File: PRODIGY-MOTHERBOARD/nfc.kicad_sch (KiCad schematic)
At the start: 1 part, among them U14 PN5321A3HN_C1xx

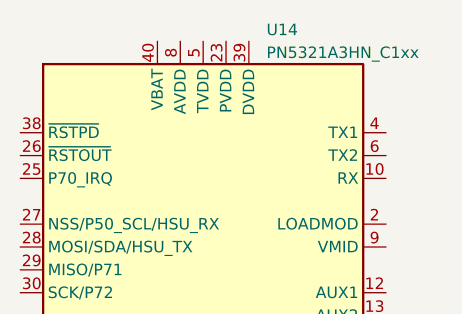
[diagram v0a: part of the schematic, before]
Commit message: project restructure done. Hierarchical sheet done. Outputs/breakouts sheet done
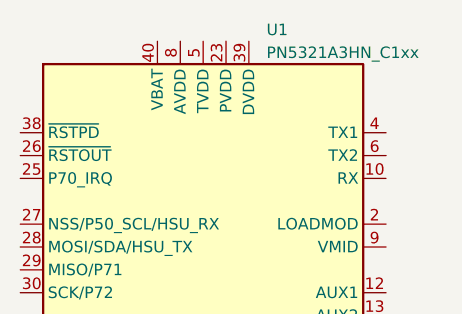
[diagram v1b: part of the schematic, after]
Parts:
- renumbered U14 to U1
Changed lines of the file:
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@@
-(kicad_sch (version 20230121) (generator eeschema)
-  (paper "A4")
-  (symbol (lib_id "RF_NFC:PN5321A3HN_C1xx") (at 148.59 95.25 0) (unit 1)
-    (in_bom yes) (on_board yes) (dnp no) (fields_autoplaced)
-    (property "Reference" "U14" (at 155.6259 60.96 0)
-      (effects (font (size 1.27 1.27)) (justify left))
-    )
-    (property "Value" "PN5321A3HN_C1xx" (at 155.6259 63.5 0)
-      (effects (font (size 1.27 1.27)) (justify left))
-    )
-    (property "Footprint" "Package_DFN_QFN:HVQFN-40-1EP_6x6mm_P0.5mm_EP4.1x4.1mm" (at 186.69 127 0)
-      (effects (font (size 1.27 1.27)) hide)
-    )
-    (property "Datasheet" "https://www.nxp.com/docs/en/nxp/data-sheets/PN532_C1.pdf" (at 148.59 90.17 0)
-      (effects (font (size 1.27 1.27)) hide)
-    )
-    (pin "1")
-    (pin "10")
-    (pin "11")
-    (pin "12")
-    (pin "13")
-    (pin "14")
-    (pin "15")
-    (pin "16")
-    (pin "17")
-    (pin "18")
-    (pin "19")
-    (pin "2")
-    (pin "20")
-    (pin "21")
-    (pin "22")
-    (pin "23")
-    (pin "24")
-    (pin "25")
-    (pin "26")
-    (pin "27")
-    (pin "28")
-    (pin "29")
-    (pin "3")
-    (pin "30")
-    (pin "31")
-    (pin "32")
-    (pin "33")
-    (pin "34")
-    (pin "35")
-    (pin "36")
-    (pin "37")
-    (pin "38")
-    (pin "39")
-    (pin "4")
-    (pin "40")
-    (pin "41")
-    (pin "5")
-    (pin "6")
-    (pin "7")
-    (pin "8")
-    (pin "9")
-    (instances
-      (project "PRODIGY-MOTHERBOARD"
-        (path "/f1c25860-8989-4190-bd24-2491d23ca7d9/edf7e11a-2a6c-4bff-b9f6-56b011438f63"
-          (reference "U14") (unit 1)
-        )
-      )
-    )
-  )
+(kicad_sch
+	(version 20231120)
+	(generator "eeschema")
+	(generator_version "8.0")
+	(paper "A4")
+	(symbol
+		(lib_id "RF_NFC:PN5321A3HN_C1xx")
+		(at 148.59 95.25 0)
+		(unit 1)
+		(exclude_from_sim no)
+		(in_bom yes)
+		(on_board yes)
+		(dnp no)
+		(fields_autoplaced yes)
+		(property "Reference" "U1"
+			(at 155.6259 60.96 0)
+			(effects
+				(font
+					(size 1.27 1.27)
+				)
+				(justify left)
+			)
+		)
+		(property "Value" "PN5321A3HN_C1xx"
+			(at 155.6259 63.5 0)
+			(effects
+				(font
+					(size 1.27 1.27)
+				)
+				(justify left)
+			)
+		)
+		(property "Footprint" "Package_DFN_QFN:HVQFN-40-1EP_6x6mm_P0.5mm_EP4.1x4.1mm"
+			(at 186.69 127 0)
+			(effects
+				(font
+					(size 1.27 1.27)
+				)
+				(hide yes)
+			)
+		)
+		(property "Datasheet" "https://www.nxp.com/docs/en/nxp/data-sheets/PN532_C1.pdf"
+			(at 148.59 90.17 0)
+			(effects
+				(font
+					(size 1.27 1.27)
+				)
+				(hide yes)
+			)
+		)
+		(property "Description" ""
+			(at 148.59 95.25 0)
+			(effects
+				(font
+					(size 1.27 1.27)
+				)
+				(hide yes)
+			)
+		)
+		(pin "1"
+		)
+		(pin "10"
+		)
+		(pin "11"
+		)
+		(pin "12"
+		)
+		(pin "13"
+		)
+		(pin "14"
+		)
+		(pin "15"
+		)
+		(pin "16"
+		)
+		(pin "17"
+		)
+		(pin "18"
+		)
+		(pin "19"
+		)
+		(pin "2"
+		)
+		(pin "20"
+		)
+		(pin "21"
+		)
+		(pin "22"
+		)
+		(pin "23"
+		)
+		(pin "24"
+		)
+		(pin "25"
+		)
+		(pin "26"
+		)
+		(pin "27"
+		)
+		(pin "28"
+		)
+		(pin "29"
+		)
+		(pin "3"
+		)
+		(pin "30"
+		)
+		(pin "31"
+		)
+		(pin "32"
+		)
+		(pin "33"
+		)
+		(pin "34"
+		)
+		(pin "35"
+		)
+		(pin "36"
+		)
+		(pin "37"
+		)
+		(pin "38"
+		)
+		(pin "39"
+		)
+		(pin "4"
+		)
+		(pin "40"
+		)
+		(pin "41"
+		)
+		(pin "5"
+		)
+		(pin "6"
+		)
+		(pin "7"
+		)
+		(pin "8"
+		)
+		(pin "9"
+		)
+		(instances
+			(project "PRODIGY-MOTHERBOARD"
+				(path "/f1c25860-8989-4190-bd24-2491d23ca7d9/e2913798-f444-47a6-8b64-53020d7d816b/f75fe182-3b01-43c3-81e9-1a0709fd1be7"
+					(reference "U1")
+					(unit 1)
+				)
+			)
+		)
+	)
 )

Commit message: CAN schematic done
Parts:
- renumbered U1 to U3
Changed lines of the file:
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@@
 		(dnp no)
 		(fields_autoplaced yes)
-		(property "Reference" "U1"
+		(property "Reference" "U3"
 			(at 155.6259 60.96 0)
 			(effects
@@
 			(project "PRODIGY-MOTHERBOARD"
 				(path "/f1c25860-8989-4190-bd24-2491d23ca7d9/e2913798-f444-47a6-8b64-53020d7d816b/f75fe182-3b01-43c3-81e9-1a0709fd1be7"
-					(reference "U1")
+					(reference "U3")
 					(unit 1)
 				)

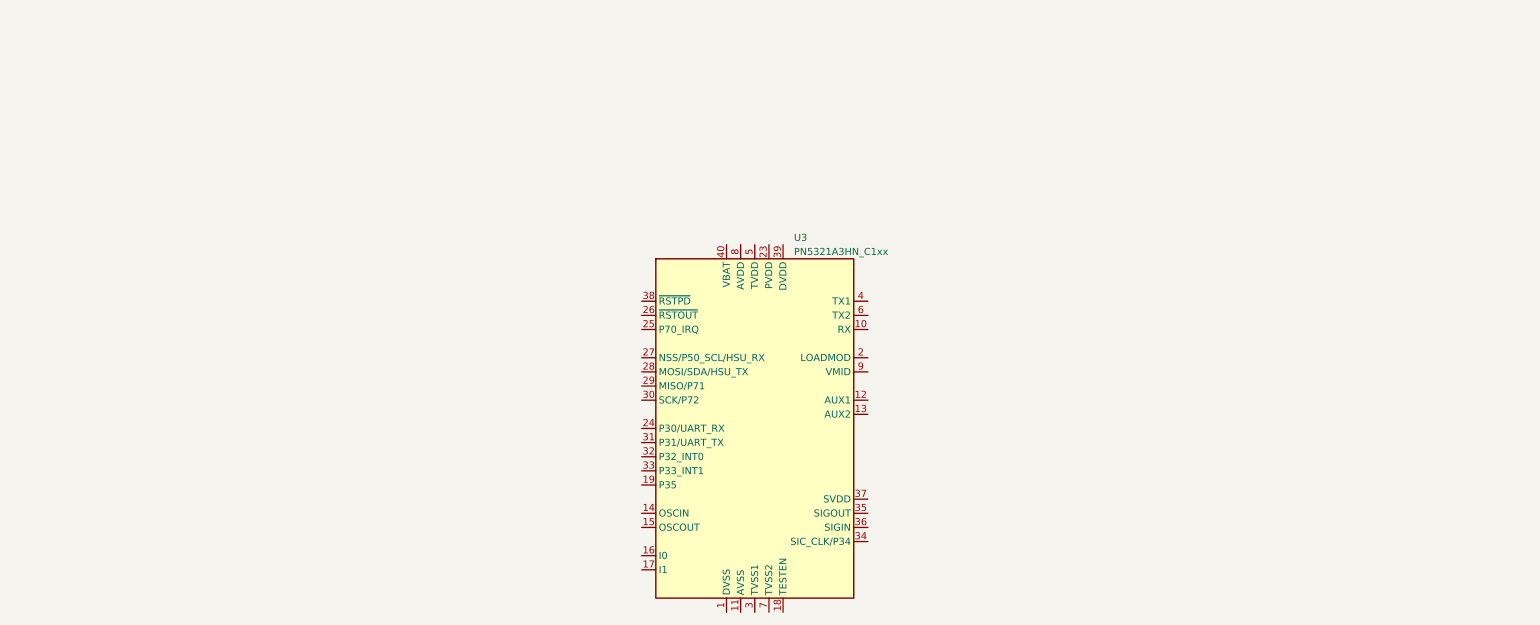
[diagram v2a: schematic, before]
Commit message: SPI NFC schematic done.
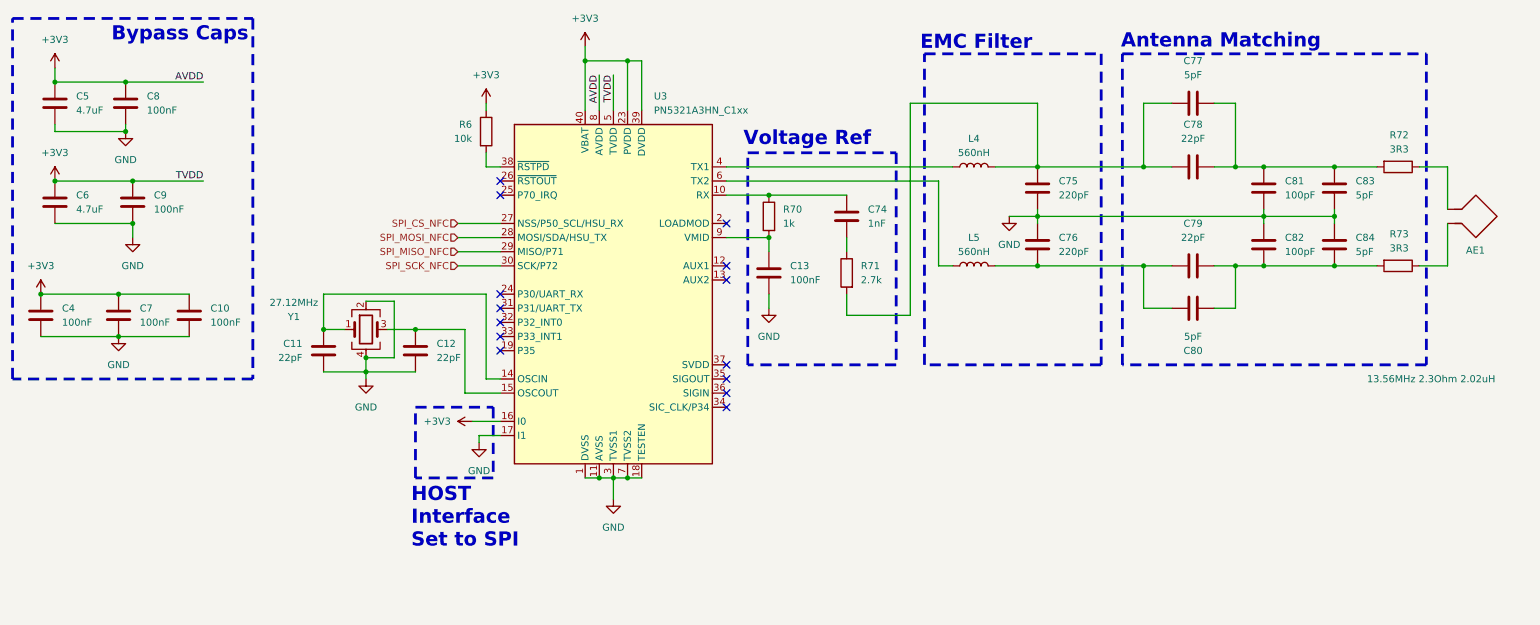
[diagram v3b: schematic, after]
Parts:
- added AE1: 13.56MHz 2.3Ohm 2.02uH, symbol Device:Antenna_Loop
- added C10, C13, C4, C7, C8, C9: 100nF, symbol Device:C
- added C11, C12, C78, C79: 22pF, symbol Device:C
- added C5, C6: 4.7uF, symbol Device:C
- added C74: 1nF, symbol Device:C
- added C75, C76: 220pF, symbol Device:C
- added C77, C80, C83, C84: 5pF, symbol Device:C
- added C81, C82: 100pF, symbol Device:C
- added L4, L5: 560nH, symbol Device:L
- added R6: 10k, symbol Device:R
- added R70: 1k, symbol Device:R
- added R71: 2.7k, symbol Device:R
- added R72, R73: 3R3, symbol Device:R
- added Y1: 27.12MHz, symbol Device:Crystal_GND24
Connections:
- net GND: now reaches U3.1 (DVSS)
- net GND: now also U3.11 (AVSS), U3.17 (I1), U3.18 (TESTEN), U3.3 (TVSS1), U3.41 (AVSS), U3.7 (TVSS2), C10.2, C11.2, C12.2, C13.2, C4.2, C5.2, C6.2, C7.2, C75.2, C76.1, C8.2, C81.2, C82.1, C83.2, C84.1, C9.2, Y1.2, Y1.4
- net at U3.10 (RX): now also C74.1, R70.1
- net at U3.14 (OSCIN): now also C11.1, Y1.1
- net at U3.15 (OSCOUT): now also C12.1, Y1.3
- net +3V3: now reaches U3.16 (I0)
- net +3V3: now also U3.23 (PVDD), U3.39 (DVDD), U3.40 (VBAT), U3.5 (TVDD), U3.8 (AVDD), C10.1, C4.1, C5.1, C6.1, C7.1, C8.1, C9.1, R6.1
- net SPI_CS_NFC: now reaches U3.27 (NSS/P50_SCL/HSU_RX)
- net SPI_MOSI_NFC: now reaches U3.28 (MOSI/SDA/HSU_TX)
- net SPI_MISO_NFC: now reaches U3.29 (MISO/P71)
- net SPI_SCK_NFC: now reaches U3.30 (SCK/P72)
- net at U3.38 (~{RSTPD}): now also R6.2
- net at U3.4 (TX1): now also L4.1
- net at U3.6 (TX2): now also L5.1
- net at U3.9 (VMID): now also C13.1, R70.2
- new net: C75.1, C77.1, C78.1, L4.2, R71.2
- new net: C77.2, C78.2, C81.1, C83.1, R72.2
- new net: AE1.1, R72.1
- new net: AE1.2, R73.1
- new net: C76.2, C79.1, C80.1, L5.2
- new net: C79.2, C80.2, C82.2, C84.2, R73.2
- new net: C74.2, R71.1
- no-connect marks 0 -> 14
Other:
- note added: "Antenna Matching"
- note added: "Bypass Caps"
- note added: "EMC Filter"
- note added: "HOST Interface Set to SPI"
- note added: "Voltage Ref"
- moved on the sheet: U3

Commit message: Added proper debounce filter elements to buttons.
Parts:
- renumbered C83 to C10, C6 to C11, C9 to C12, C74 to C13, C76 to C14, C82 to C15, C84 to C16, C79 to C17, C13 to C18, C80 to C19, C4 to C20, C7 to C21, C10 to C22, C11 to C23, C12 to C24, C5 to C4, C8 to C5, C77 to C6, C78 to C7, C75 to C8, C81 to C9, L4 to L1, L5 to L2, R71 to R10, R72 to R7, R70 to R8, R73 to R9

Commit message: Submitted V0 for evaluation. Avaiting feedback.
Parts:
- renumbered R9 to R10, R10 to R11, R6 to R7, R7 to R8, R8 to R9, U3 to U4
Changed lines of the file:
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@@
 		(dnp no)
 		(fields_autoplaced yes)
-		(property "Reference" "#PWR024"
+		(property "Reference" "#PWR048"
 			(at 100.33 40.64 0)
 			(effects
@@
 			(project "PRODIGY-MOTHERBOARD"
 				(path "/f1c25860-8989-4190-bd24-2491d23ca7d9/e2913798-f444-47a6-8b64-53020d7d816b/d8aab2a1-25b6-4fb2-8368-6cdabd5442db"
-					(reference "#PWR024")
+					(reference "#PWR048")
 					(unit 1)
 				)
@@
 		(dnp no)
 		(fields_autoplaced yes)
-		(property "Reference" "#PWR022"
+		(property "Reference" "#PWR046"
 			(at 118.11 30.48 0)
 			(effects
@@
 			(project "PRODIGY-MOTHERBOARD"
 				(path "/f1c25860-8989-4190-bd24-2491d23ca7d9/e2913798-f444-47a6-8b64-53020d7d816b/d8aab2a1-25b6-4fb2-8368-6cdabd5442db"
-					(reference "#PWR022")
+					(reference "#PWR046")
 					(unit 1)
 				)
@@
 		(on_board yes)
 		(dnp no)
-		(property "Reference" "R7"
+		(property "Reference" "R8"
 			(at 266.065 42.5449 90)
 			(effects
@@
 			(project "PRODIGY-MOTHERBOARD"
 				(path "/f1c25860-8989-4190-bd24-2491d23ca7d9/e2913798-f444-47a6-8b64-53020d7d816b/d8aab2a1-25b6-4fb2-8368-6cdabd5442db"
-					(reference "R7")
+					(reference "R8")
 					(unit 1)
 				)
@@
 		(dnp no)
 		(fields_autoplaced yes)
-		(property "Reference" "#PWR035"
+		(property "Reference" "#PWR059"
 			(at 123.19 114.3 0)
 			(effects
@@
 			(project "PRODIGY-MOTHERBOARD"
 				(path "/f1c25860-8989-4190-bd24-2491d23ca7d9/e2913798-f444-47a6-8b64-53020d7d816b/d8aab2a1-25b6-4fb2-8368-6cdabd5442db"
-					(reference "#PWR035")
+					(reference "#PWR059")
 					(unit 1)
 				)
@@
 		(on_board yes)
 		(dnp no)
-		(property "Reference" "R10"
+		(property "Reference" "R11"
 			(at 167.64 66.0399 0)
 			(effects
@@
 			(project "PRODIGY-MOTHERBOARD"
 				(path "/f1c25860-8989-4190-bd24-2491d23ca7d9/e2913798-f444-47a6-8b64-53020d7d816b/d8aab2a1-25b6-4fb2-8368-6cdabd5442db"
-					(reference "R10")
+					(reference "R11")
 					(unit 1)
 				)
@@
 		(on_board yes)
 		(dnp no)
-		(property "Reference" "R6"
+		(property "Reference" "R7"
 			(at 97.79 40.6399 0)
 			(effects
@@
 			(project "PRODIGY-MOTHERBOARD"
 				(path "/f1c25860-8989-4190-bd24-2491d23ca7d9/e2913798-f444-47a6-8b64-53020d7d816b/d8aab2a1-25b6-4fb2-8368-6cdabd5442db"
-					(reference "R6")
+					(reference "R7")
 					(unit 1)
 				)
@@
 		(dnp no)
 		(fields_autoplaced yes)
-		(property "Reference" "#PWR027"
+		(property "Reference" "#PWR051"
 			(at 194.31 63.5 0)
 			(effects
@@
 			(project "PRODIGY-MOTHERBOARD"
 				(path "/f1c25860-8989-4190-bd24-2491d23ca7d9/e2913798-f444-47a6-8b64-53020d7d816b/d8aab2a1-25b6-4fb2-8368-6cdabd5442db"
-					(reference "#PWR027")
+					(reference "#PWR051")
 					(unit 1)
 				)
@@
 		(dnp no)
 		(fields_autoplaced yes)
-		(property "Reference" "#PWR029"
+		(property "Reference" "#PWR053"
 			(at 20.32 74.93 0)
 			(effects
@@
 			(project "PRODIGY-MOTHERBOARD"
 				(path "/f1c25860-8989-4190-bd24-2491d23ca7d9/e2913798-f444-47a6-8b64-53020d7d816b/d8aab2a1-25b6-4fb2-8368-6cdabd5442db"
-					(reference "#PWR029")
+					(reference "#PWR053")
 					(unit 1)
 				)
@@
 		(on_board yes)
 		(dnp no)
-		(property "Reference" "R8"
+		(property "Reference" "R9"
 			(at 153.67 55.8799 0)
 			(effects
@@
 			(project "PRODIGY-MOTHERBOARD"
 				(path "/f1c25860-8989-4190-bd24-2491d23ca7d9/e2913798-f444-47a6-8b64-53020d7d816b/d8aab2a1-25b6-4fb2-8368-6cdabd5442db"
-					(reference "R8")
+					(reference "R9")
 					(unit 1)
 				)
@@
 		(dnp no)
 		(fields_autoplaced yes)
-		(property "Reference" "#PWR033"
+		(property "Reference" "#PWR057"
 			(at 101.6 93.98 0)
 			(effects
@@
 			(project "PRODIGY-MOTHERBOARD"
 				(path "/f1c25860-8989-4190-bd24-2491d23ca7d9/e2913798-f444-47a6-8b64-53020d7d816b/d8aab2a1-25b6-4fb2-8368-6cdabd5442db"
-					(reference "#PWR033")
+					(reference "#PWR057")
 					(unit 1)
 				)
@@
 		(dnp no)
 		(fields_autoplaced yes)
-		(property "Reference" "#PWR034"
+		(property "Reference" "#PWR058"
 			(at 99.06 104.14 0)
 			(effects
@@
 			(project "PRODIGY-MOTHERBOARD"
 				(path "/f1c25860-8989-4190-bd24-2491d23ca7d9/e2913798-f444-47a6-8b64-53020d7d816b/d8aab2a1-25b6-4fb2-8368-6cdabd5442db"
-					(reference "#PWR034")
+					(reference "#PWR058")
 					(unit 1)
 				)
@@
 		(dnp no)
 		(fields_autoplaced yes)
-		(property "Reference" "#PWR025"
+		(property "Reference" "#PWR049"
 			(at 35.56 48.26 0)
 			(effects
@@
 			(project "PRODIGY-MOTHERBOARD"
 				(path "/f1c25860-8989-4190-bd24-2491d23ca7d9/e2913798-f444-47a6-8b64-53020d7d816b/d8aab2a1-25b6-4fb2-8368-6cdabd5442db"
-					(reference "#PWR025")
+					(reference "#PWR049")
 					(unit 1)
 				)
@@
 		(dnp no)
 		(fields_autoplaced yes)
-		(property "Reference" "U3"
+		(property "Reference" "U4"
 			(at 130.4641 35.56 0)
 			(effects
@@
 			(project "PRODIGY-MOTHERBOARD"
 				(path "/f1c25860-8989-4190-bd24-2491d23ca7d9/e2913798-f444-47a6-8b64-53020d7d816b/d8aab2a1-25b6-4fb2-8368-6cdabd5442db"
-					(reference "U3")
+					(reference "U4")
 					(unit 1)
 				)
@@
 		(dnp no)
 		(fields_autoplaced yes)
-		(property "Reference" "#PWR026"
+		(property "Reference" "#PWR050"
 			(at 22.86 54.61 0)
 			(effects
@@
 			(project "PRODIGY-MOTHERBOARD"
 				(path "/f1c25860-8989-4190-bd24-2491d23ca7d9/e2913798-f444-47a6-8b64-53020d7d816b/d8aab2a1-25b6-4fb2-8368-6cdabd5442db"
-					(reference "#PWR026")
+					(reference "#PWR050")
 					(unit 1)
 				)
@@
 		(dnp no)
 		(fields_autoplaced yes)
-		(property "Reference" "#PWR032"
+		(property "Reference" "#PWR056"
 			(at 78.74 92.71 0)
 			(effects
@@
 			(project "PRODIGY-MOTHERBOARD"
 				(path "/f1c25860-8989-4190-bd24-2491d23ca7d9/e2913798-f444-47a6-8b64-53020d7d816b/d8aab2a1-25b6-4fb2-8368-6cdabd5442db"
-					(reference "#PWR032")
+					(reference "#PWR056")
 					(unit 1)
 				)
@@
 		(dnp no)
 		(fields_autoplaced yes)
-		(property "Reference" "#PWR023"
+		(property "Reference" "#PWR047"
 			(at 22.86 34.29 0)
 			(effects
@@
 			(project "PRODIGY-MOTHERBOARD"
 				(path "/f1c25860-8989-4190-bd24-2491d23ca7d9/e2913798-f444-47a6-8b64-53020d7d816b/d8aab2a1-25b6-4fb2-8368-6cdabd5442db"
-					(reference "#PWR023")
+					(reference "#PWR047")
 					(unit 1)
 				)
@@
 		(dnp no)
 		(fields_autoplaced yes)
-		(property "Reference" "#PWR028"
+		(property "Reference" "#PWR052"
 			(at 36.83 67.31 0)
 			(effects
@@
 			(project "PRODIGY-MOTHERBOARD"
 				(path "/f1c25860-8989-4190-bd24-2491d23ca7d9/e2913798-f444-47a6-8b64-53020d7d816b/d8aab2a1-25b6-4fb2-8368-6cdabd5442db"
-					(reference "#PWR028")
+					(reference "#PWR052")
 					(unit 1)
 				)
@@
 		(dnp no)
 		(fields_autoplaced yes)
-		(property "Reference" "#PWR030"
+		(property "Reference" "#PWR054"
 			(at 151.13 80.01 0)
 			(effects
@@
 			(project "PRODIGY-MOTHERBOARD"
 				(path "/f1c25860-8989-4190-bd24-2491d23ca7d9/e2913798-f444-47a6-8b64-53020d7d816b/d8aab2a1-25b6-4fb2-8368-6cdabd5442db"
-					(reference "#PWR030")
+					(reference "#PWR054")
 					(unit 1)
 				)
@@
 		(on_board yes)
 		(dnp no)
-		(property "Reference" "R9"
+		(property "Reference" "R10"
 			(at 266.065 60.3249 90)
 			(effects
@@
 			(project "PRODIGY-MOTHERBOARD"
 				(path "/f1c25860-8989-4190-bd24-2491d23ca7d9/e2913798-f444-47a6-8b64-53020d7d816b/d8aab2a1-25b6-4fb2-8368-6cdabd5442db"
-					(reference "R9")
+					(reference "R10")
 					(unit 1)
 				)
@@
 		(dnp no)
 		(fields_autoplaced yes)
-		(property "Reference" "#PWR031"
+		(property "Reference" "#PWR055"
 			(at 34.29 85.09 0)
 			(effects
@@
 			(project "PRODIGY-MOTHERBOARD"
 				(path "/f1c25860-8989-4190-bd24-2491d23ca7d9/e2913798-f444-47a6-8b64-53020d7d816b/d8aab2a1-25b6-4fb2-8368-6cdabd5442db"
-					(reference "#PWR031")
-					(unit 1)
-				)
+					(reference "#PWR055")
+					(unit 1)
+				)

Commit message: MCU schematic done. Started Analog design.
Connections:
- net SPI_IRQ_NFC: now reaches U4.25 (P70_IRQ)
- net SPI_RST_NFC: now reaches U4.26 (~{RSTOUT})
- no-connect marks 14 -> 12
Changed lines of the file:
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@@
 	)
 	(no_connect
-		(at 102.87 53.34)
-	)
-	(no_connect
 		(at 143.51 68.58)
 	)
@@
 	)
 	(no_connect
-		(at 102.87 50.8)
-	)
-	(no_connect
 		(at 143.51 83.82)
 	)
@@
 	(wire
 		(pts
+			(xy 95.25 53.34) (xy 102.87 53.34)
+		)
+		(stroke
+			(width 0)
+			(type default)
+		)
+	)
+	(wire
+		(pts
 			(xy 22.86 58.42) (xy 36.83 58.42)
 		)
@@
 	(wire
 		(pts
+			(xy 95.25 50.8) (xy 102.87 50.8)
+		)
+		(stroke
+			(width 0)
+			(type default)
+		)
+	)
+	(wire
+		(pts
 			(xy 36.83 50.8) (xy 49.53 50.8)
 		)
@@
 		)
 	)
+	(hierarchical_label "SPI_RST_NFC"
+		(shape input)
+		(at 95.25 50.8 180)
+		(fields_autoplaced yes)
+		(effects
+			(font
+				(size 1.27 1.27)
+			)
+			(justify right)
+		)
+	)
 	(hierarchical_label "SPI_MISO_NFC"
 		(shape input)
@@
 		(fields_autoplaced yes)
 		(effects
+			(font
+				(size 1.27 1.27)
+			)
+			(justify right)
+		)
+	)
+	(hierarchical_label "SPI_IRQ_NFC"
+		(shape input)
+		(at 95.25 53.34 180)
+		(fields_autoplaced yes)
+		(effects

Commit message: Finished v0.1 schematic.
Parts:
- added FID15, FID16: Fiducial, symbol Mechanical:Fiducial
- renumbered C20 to C44, C4 to C45, C11 to C46, C21 to C47, C5 to C48, C12 to C49, C22 to C50, C23 to C51, C24 to C52, C18 to C53, C13 to C54, C8 to C55, C14 to C56, C6 to C57, C7 to C58, C17 to C59, C19 to C60, C9 to C61, C15 to C62, C10 to C63, C16 to C64, L1 to L5, L2 to L6, R7 to R33, R9 to R34, R11 to R35, R8 to R36, R10 to R37, U4 to U16

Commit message: schematic v0.2 finalized
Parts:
- renumbered C44 to C43, C45 to C44, C46 to C45, C47 to C46, C48 to C47, C49 to C48, C50 to C49, C51 to C50, C52 to C51, C53 to C52, C54 to C53, C55 to C54, C56 to C55, C57 to C56, C58 to C57, C59 to C58, C60 to C59, C61 to C60, C62 to C61, C63 to C62, C64 to C63, FID15 to FID17, FID16 to FID18
